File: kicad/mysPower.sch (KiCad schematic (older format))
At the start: 12 parts, among them P1 CNX2, P2 CNX2, P9 CONN_01X06, Q1 BS170, U1 ArduinoNano, U2 NRF24L01, U3 LTV-814

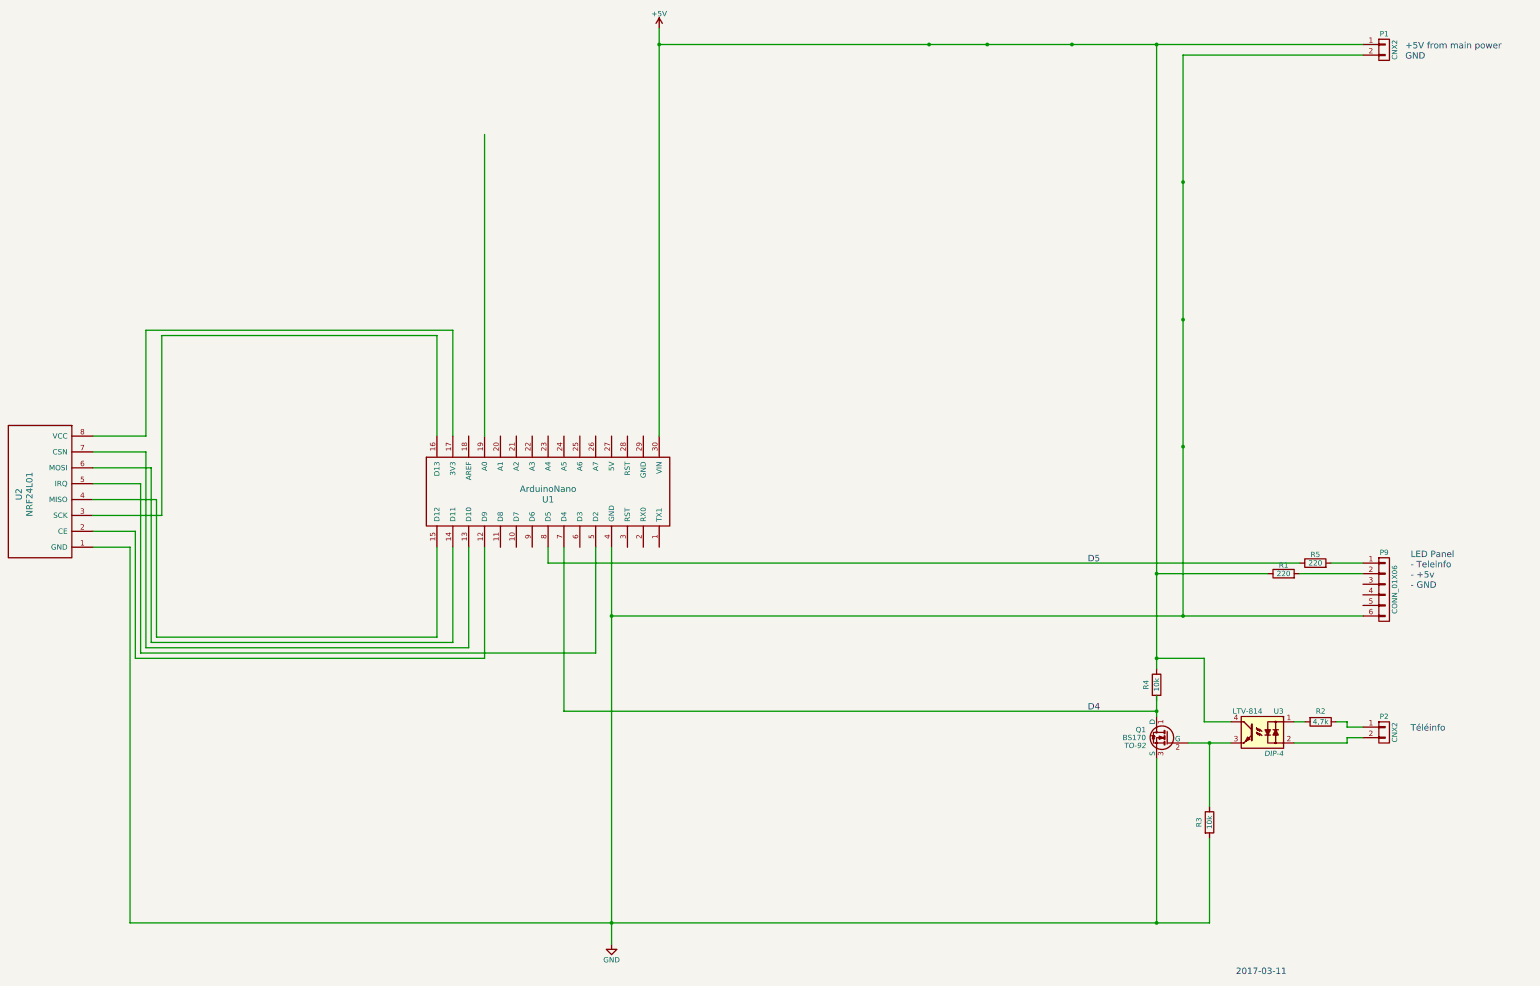
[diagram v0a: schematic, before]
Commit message: Add HC/HP LEDs (todo #1)
+ allow any LED to be ignored via pin=0.
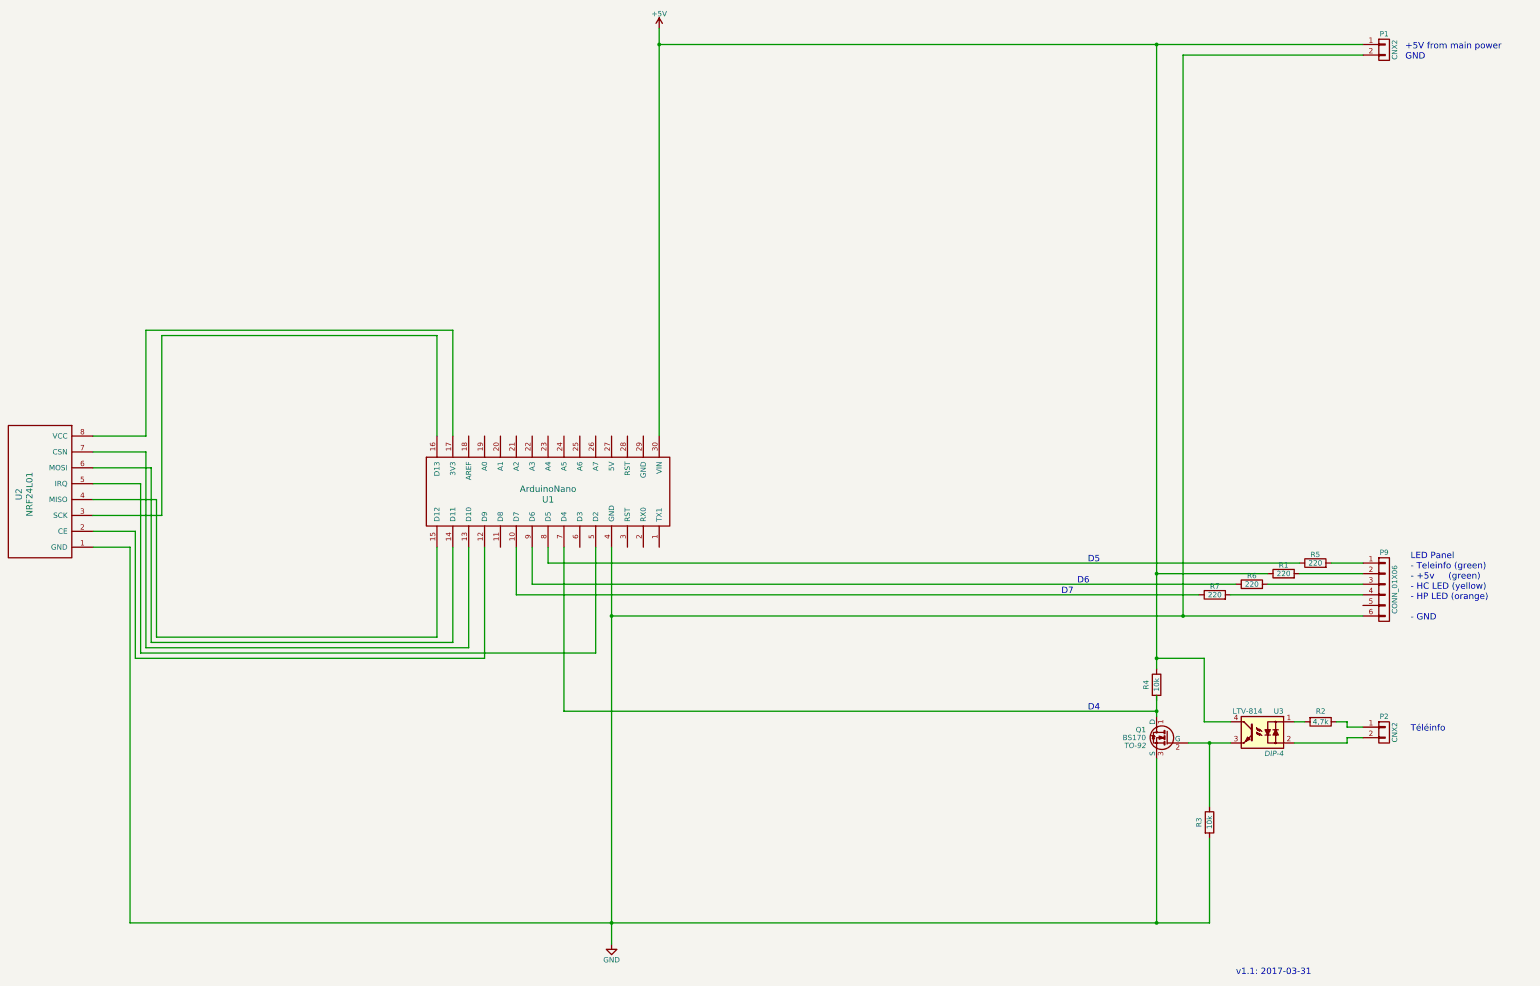
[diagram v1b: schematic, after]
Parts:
- added R6, R7: 220, symbol R
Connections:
- wire segments 78 -> 66
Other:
- note added: "D6"
- note added: "D7"
- note added: "LED Panel\n- Teleinfo (green)\n- +5v (green)\n- HC LED (yellow)\n- HP LED (orange)\n\n- GND"
- note added: "v1.1: 2017-03-31"
- note removed: "2017-03-11"
- note removed: "LED Panel\n- Teleinfo\n- +5v\n- GND"
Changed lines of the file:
@@
 $EndComp
 Text Notes 13400 10200 0    60   ~ 0
-2017-03-11
+v1.1: 2017-03-31
 $Comp
 L CONN_01X02 P2
@@
 	14050 7800 13950 7800
 Wire Wire Line
-	12950 8000 13150 8000
-Wire Wire Line
-	13150 8000 13350 8000
+	12950 8000 13350 8000
 Connection ~ 13150 8000
 Wire Wire Line
-	12650 1400 12650 6400
-Wire Wire Line
-	12650 6400 12650 7200
-Wire Wire Line
-	12650 7200 12650 7300
+	12650 1400 12650 7300
 Wire Wire Line
 	12650 7200 13100 7200
@@
 	2950 6150 2950 9700
 Wire Wire Line
-	2950 9700 7500 9700
-Wire Wire Line
-	7500 9700 12650 9700
-Wire Wire Line
-	12650 9700 13150 9700
-Wire Wire Line
-	7500 6150 7500 6800
-Wire Wire Line
-	7500 6800 7500 9700
-Wire Wire Line
-	7500 9700 7500 9900
+	2950 9700 13150 9700
+Wire Wire Line
+	7500 6150 7500 9900
 Wire Wire Line
 	13950 8000 14450 8000
@@
 	14450 7850 14600 7850
 Wire Wire Line
-	7950 1400 10500 1400
-Wire Wire Line
-	10500 1400 11050 1400
-Wire Wire Line
-	11050 1400 11850 1400
-Wire Wire Line
-	11850 1400 12650 1400
-Wire Wire Line
-	12650 1400 14600 1400
-Wire Wire Line
-	7950 1250 7950 1400
-Wire Wire Line
-	7950 1400 7950 5100
+	7950 1400 14600 1400
+Wire Wire Line
+	7950 1250 7950 5100
 Connection ~ 7950 1400
 Wire Wire Line
-	12650 7550 12650 7700
-Wire Wire Line
-	12650 7700 12650 7750
+	12650 7550 12650 7750
 Wire Wire Line
 	13150 9700 13150 8900
@@
 	14300 6300 14600 6300
 Wire Wire Line
-	7500 6800 12900 6800
+	7500 6800 14600 6800
 Connection ~ 7500 6800
 Wire Wire Line
-	12900 1500 12900 2700
-Wire Wire Line
-	12900 2700 12900 4000
-Wire Wire Line
-	12900 4000 12900 5200
-Wire Wire Line
-	12900 5200 12900 6800
+	12900 1500 12900 6800
 Connection ~ 12900 6800
-Connection ~ 12900 5200
-Connection ~ 12900 4000
 Wire Wire Line
 	14600 1500 12900 1500
-Connection ~ 12900 2700
-Connection ~ 10500 1400
-Wire Wire Line
-	6300 5100 6300 2250
-Connection ~ 11050 1400
-Connection ~ 11850 1400
 Text Notes 12000 7700 0    60   ~ 0
 D4
@@
 Wire Wire Line
 	6900 6150 6900 6300
-Text Notes 15050 6550 0    60   ~ 0
-LED Panel\n- Teleinfo\n- +5v\n- GND
+Text Notes 15050 6850 0    60   ~ 0
+LED Panel\n- Teleinfo (green)\n- +5v     (green)\n- HC LED (yellow)\n- HP LED (orange)\n\n- GND
 Wire Wire Line
 	14000 6400 14600 6400
-Wire Wire Line
-	12900 6800 14600 6800
+$Comp
+L R R6
+U 1 1 58DE3F97
+P 13550 6500
+F 0 "R6" V 13630 6500 50  0000 C CNN
+F 1 "220" V 13550 6500 50  0000 C CNN
+F 2 "" V 13480 6500 50  0000 C CNN
+F 3 "" H 13550 6500 50  0000 C CNN
+	1    13550 6500
+	0    -1   -1   0
+$EndComp
+Wire Wire Line
+	13700 6500 14600 6500
+Wire Wire Line
+	6750 6150 6750 6500
+Wire Wire Line
+	6750 6500 13400 6500
+$Comp
+L R R7
+U 1 1 58DE4144
+P 13200 6600
+F 0 "R7" V 13280 6600 50  0000 C CNN
+F 1 "220" V 13200 6600 50  0000 C CNN
+F 2 "" V 13130 6600 50  0000 C CNN
+F 3 "" H 13200 6600 50  0000 C CNN
+	1    13200 6600
+	0    -1   -1   0
+$EndComp
+Wire Wire Line
+	13350 6600 14600 6600
+Wire Wire Line
+	13050 6600 6600 6600
+Wire Wire Line
+	6600 6600 6600 6150
+Text Notes 11900 6500 0    60   ~ 0
+D6
+Text Notes 11750 6600 0    60   ~ 0
+D7
 $EndSCHEMATC
